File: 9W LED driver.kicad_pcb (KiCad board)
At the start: 2 copper layers, 27 parts, among them IC1 Si 9752 680PY89

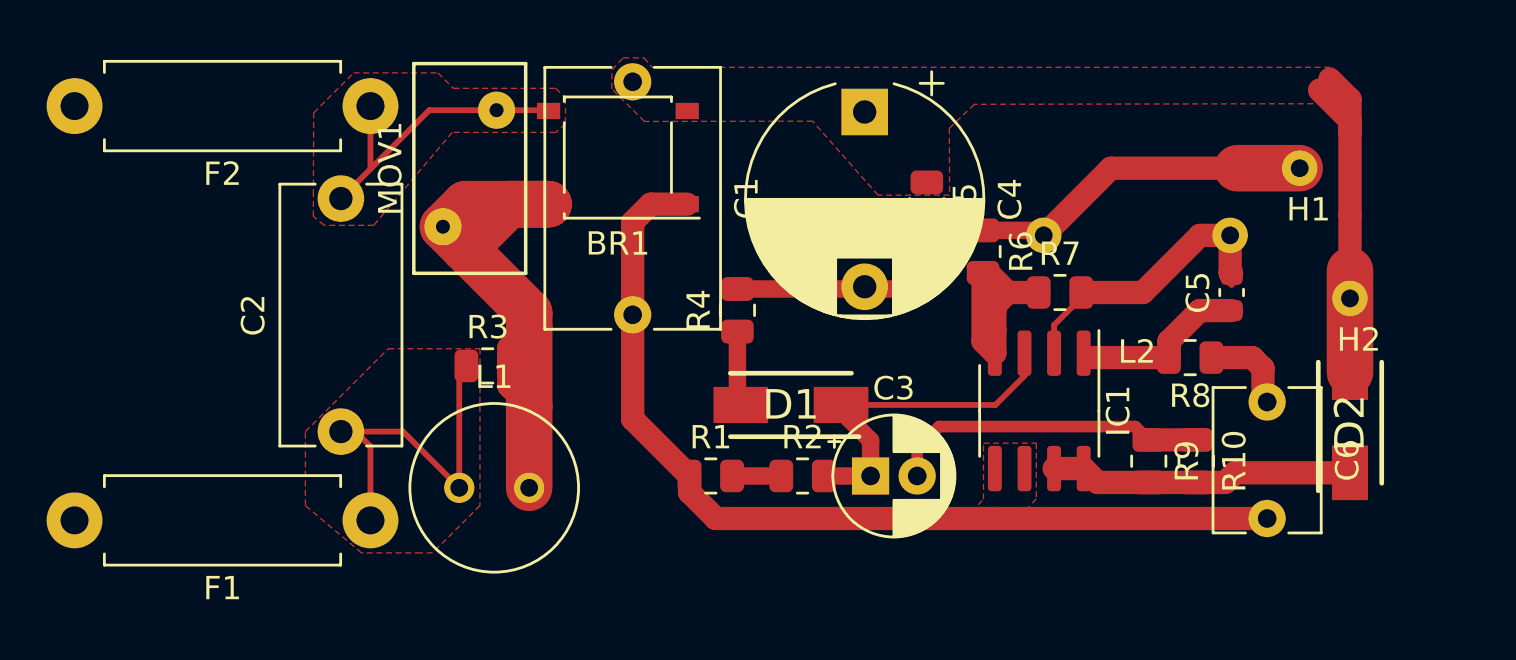
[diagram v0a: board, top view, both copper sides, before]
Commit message: Layout Fix
Fixed Layout issues and updated Silkscreen
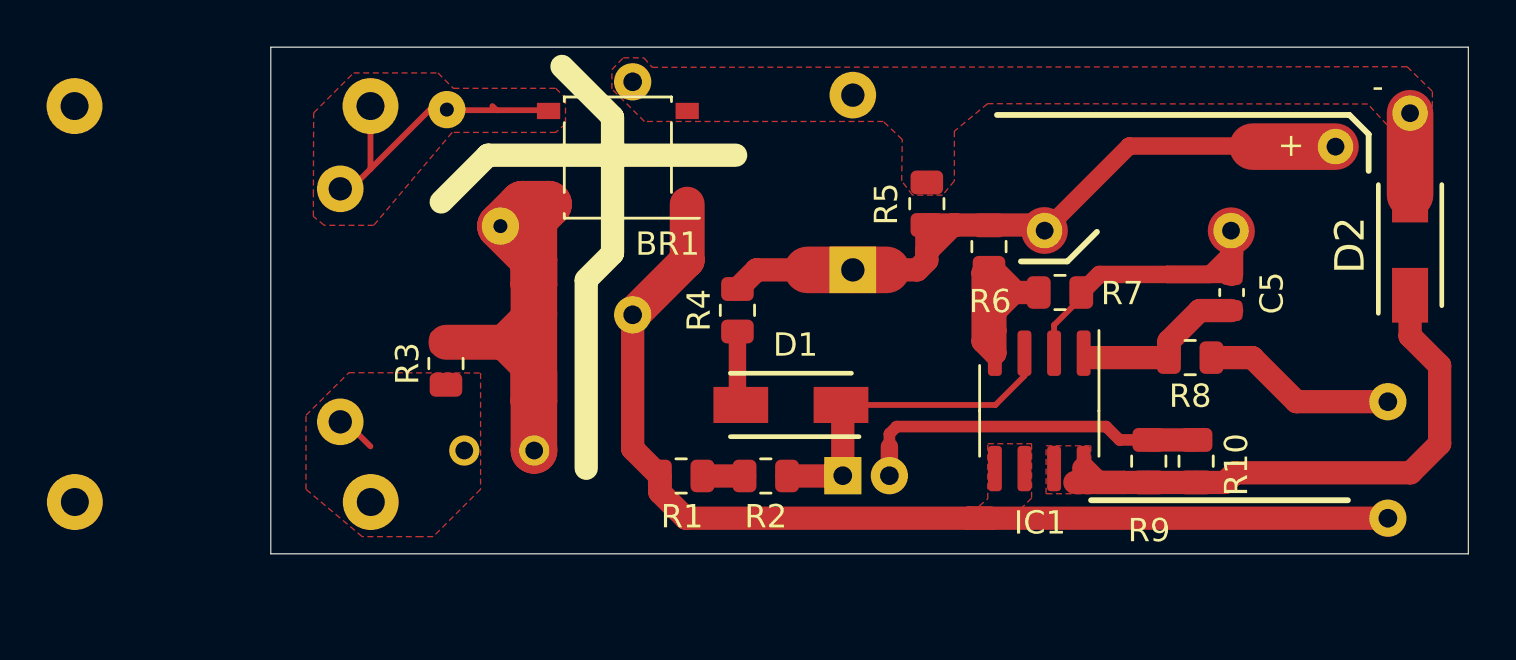
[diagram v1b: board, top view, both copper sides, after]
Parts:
- C1, C2, C3, C4, C6, F1, F2, L1, L2, MOV1: moved to B.Cu
- moved - 8.36 mm to (101.8, 53.6)
- moved D2 8.04 mm to (101.8, 59.3)
- moved C4 6.80 mm to (77.9, 60.4), turned to 90 degrees
- moved C6 5.18 mm to (100.8, 66.0)
- moved MOV1 2.13 mm to (60.4, 53.5)
- moved + 1.79 mm to (98.6, 55.1)
- moved R3 1.79 mm to (60.4, 64.4), turned to 90 degrees
- moved L1 1.61 mm to (61.2, 68.1)
- moved R2 1.58 mm to (74.1, 69.2)
- moved R1 1.27 mm to (70.5, 69.2)
- moved C3 1.19 mm to (77.4, 69.2)
- moved F1 0.79 mm to (57.2, 70.3)
- moved C2 0.42 mm to (55.9, 66.9)
- moved R6 0.33 mm to (83.7, 59.4)
- moved L2 0.21 mm to (90.1, 64.2), turned to 0 degrees
- renumbered H1 to +, H2 to -
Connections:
- C4 pad 1: -ve_Rail -> Net-(C4-Pad2)
- C4 pad 2: Net-(C4-Pad2) -> -ve_Rail
- L2 pad 1: Net-(C5-Pad2) -> Net-(C4-Pad2)
- L2 pad 2: Net-(C4-Pad2) -> Net-(C5-Pad2)
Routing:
- net Net-(C2-Pad1): track 16.1 -> 1.53 mm
- net -ve_Rail: track 17.0 -> 3.58 mm
- net Net-(D2-Pad1): track 13.7 -> 25.2 mm
- net +ve_Rail: track 40.5 -> 46.5 mm
- net Net-(C4-Pad2): track 36.2 -> 31.1 mm
- net Net-(C6-Pad1): track 3.92 -> 8.35 mm
- net Net-(C5-Pad2): track 12.3 -> 14.9 mm
- net Net-(BR1-Pad4): track 26.5 -> 23.9 mm
- net Net-(C3-Pad2): track 14.3 -> 15.9 mm
- net Net-(IC1-Pad4): track 11.9 -> 10.8 mm
- net Net-(R1-Pad2): track 2.11 -> 1.51 mm
- added copper zone on F.Cu, net Net-(D2-Pad1)
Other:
- board outline added: 51.4 x 21.7 mm
- board text added: "+"
- board text added: "-"
- board text added: "L"
- board text added: "N"

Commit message: refined design
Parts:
- added REF**: OSHW-Symbol_6.7x6mm_SilkScreen, Symbol:OSHW-Symbol_6.7x6mm_SilkScreen, B.Cu at (71.3, 68.6)
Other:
- board text added: "SIC9752_22082022_REV.001"
- board text added: "github.com/RandomDelta6"
